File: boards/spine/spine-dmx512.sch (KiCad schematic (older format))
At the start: 20 parts, among them CON6 XLR-3 Female, Q1 DMN3190LDW, T1 10/100baseT transformer, U3 AP2204K-5.0, U5 NC7WZ14, U6 ST485E

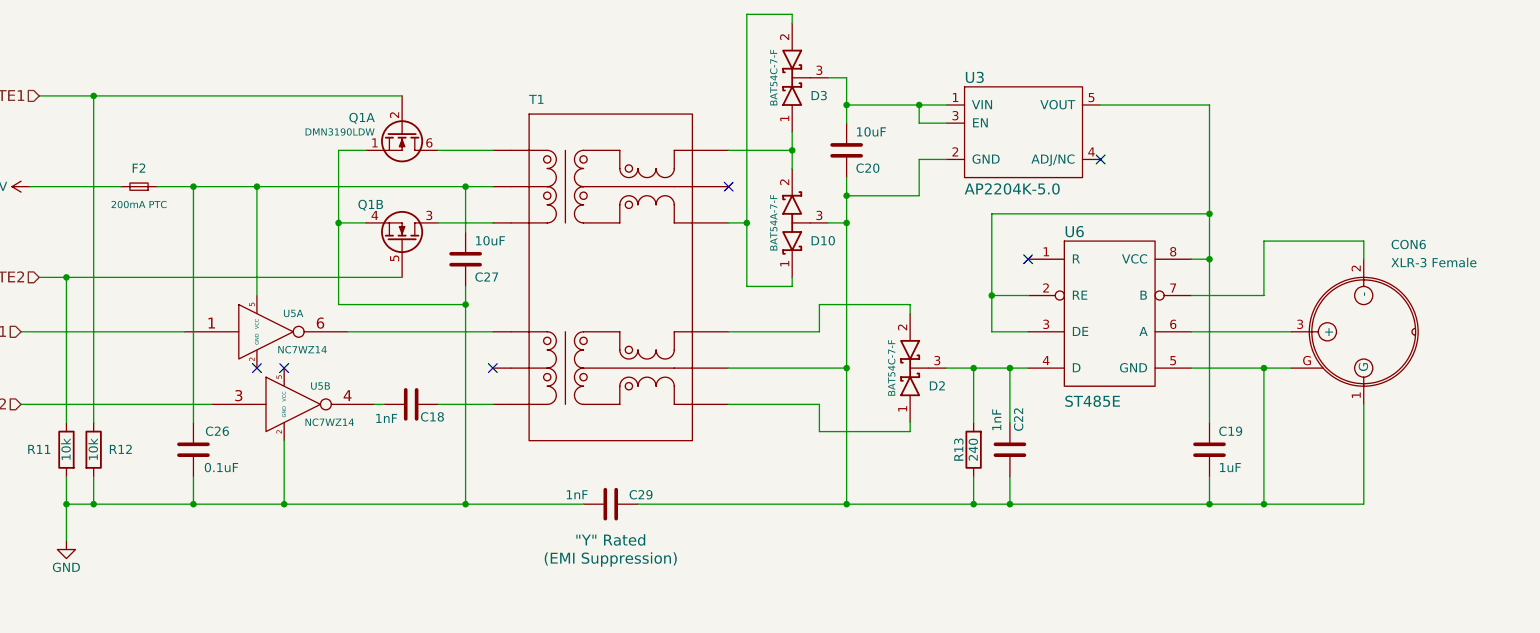
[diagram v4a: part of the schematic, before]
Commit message: Capacitor upgrades, BOM tidying
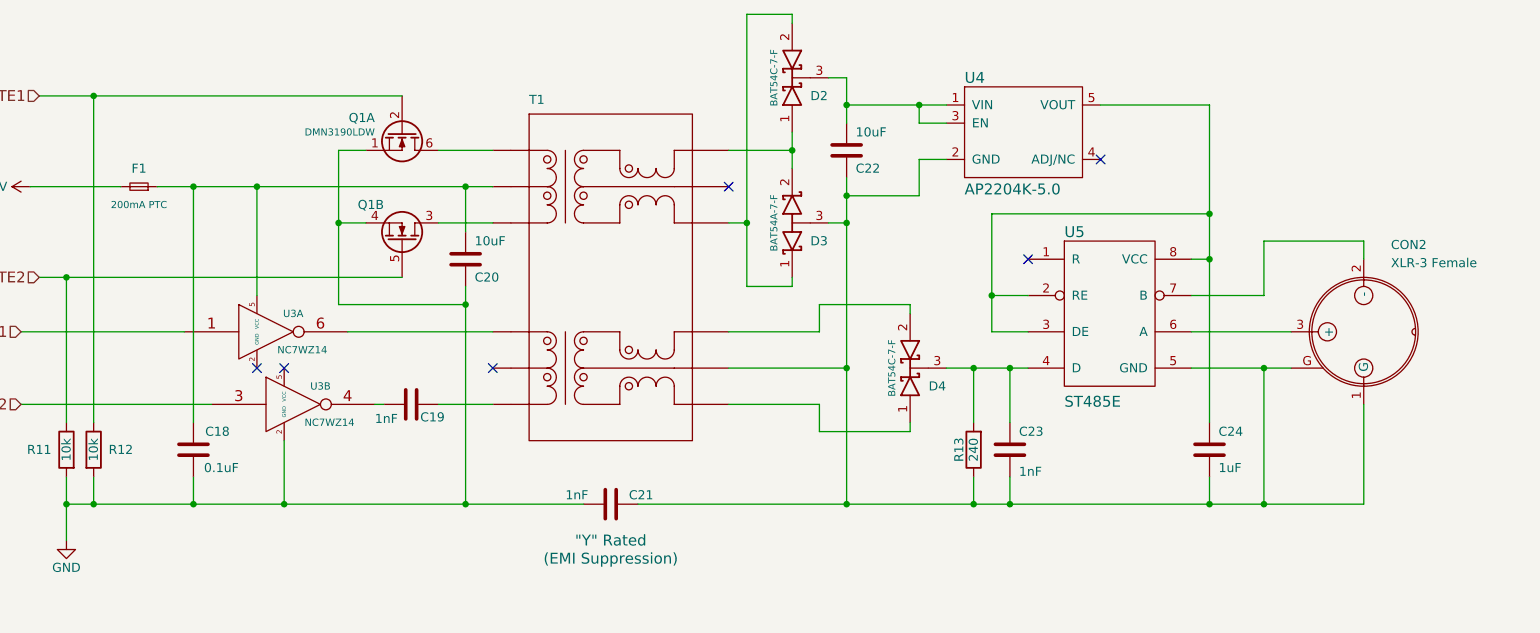
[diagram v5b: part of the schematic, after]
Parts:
- renumbered C26 to C18, C18 to C19, C27 to C20, C29 to C21, C20 to C22, C22 to C23, C19 to C24, CON6 to CON2, D3 to D2, D10 to D3, D2 to D4, F2 to F1, U5 to U3, U3 to U4, U6 to U5
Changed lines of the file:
@@
 $EndComp
 $Comp
-L C C22
+L C C23
 U 1 1 563EDC1A
 P 7200 4750
-F 0 "C22" V 7150 4850 50  0000 L CNN
-F 1 "1nF" V 7300 4850 50  0000 L BNN
+F 0 "C23" H 7150 4850 50  0000 R CNN
+F 1 "1nF" H 7150 4600 50  0000 R BNN
 F 2 "Capacitors_SMD:C_0805" H 7238 4600 30  0001 C CNN
 F 3 "http://search.murata.co.jp/Ceramy/image/img/A01X/G101/ENG/GRM216R71H102KA01-01.pdf" H 7200 4750 60  0001 C CNN
@@
 $EndComp
 $Comp
-L D_Schottky_x2_KCom_AAK D3
+L D_Schottky_x2_KCom_AAK D2
 U 1 1 563EE535
 P 6000 2700
-F 0 "D3" V 5900 2600 50  0000 R CNN
+F 0 "D2" V 5900 2600 50  0000 R CNN
 F 1 "BAT54 2x common cathode" H 6000 2800 50  0001 C CNN
 F 2 "TO_SOT_Packages_SMD:SOT-23" H 6000 2700 60  0001 C CNN
@@
 $EndComp
 $Comp
-L GND #PWR018
+L GND #PWR19
 U 1 1 563F2AEF
 P 2000 5250
-F 0 "#PWR018" H 2000 5000 50  0001 C CNN
+F 0 "#PWR19" H 2000 5000 50  0001 C CNN
 F 1 "GND" H 2000 5100 50  0000 C CNN
 F 2 "" H 2000 5250 60  0000 C CNN
@@
 TX2
 $Comp
-L NC7WZ14 U5
+L NC7WZ14 U3
 U 1 1 563F2A79
 P 3100 4100
-F 0 "U5" H 3250 4200 40  0000 C CNN
+F 0 "U3" H 3250 4200 40  0000 C CNN
 F 1 "NC7WZ14" H 3300 4000 40  0000 C CNN
 F 2 "TO_SOT_Packages_SMD:SC-70-6" H 3100 4100 60  0001 C CNN
@@
 $EndComp
 $Comp
-L NC7WZ14 U5
+L NC7WZ14 U3
 U 2 1 563F2AF3
 P 3250 4500
-F 0 "U5" H 3400 4600 40  0000 C CNN
+F 0 "U3" H 3400 4600 40  0000 C CNN
 F 1 "NC7WZ14" H 3450 4400 40  0000 C CNN
 F 2 "TO_SOT_Packages_SMD:SC-70-6" H 3250 4500 60  0001 C CNN
@@
 $EndComp
 $Comp
-L C C20
+L C C22
 U 1 1 56431ABC
 P 6300 3100
-F 0 "C20" H 6350 3000 50  0000 L CNN
+F 0 "C22" H 6350 3000 50  0000 L CNN
 F 1 "10uF" H 6350 3200 50  0000 L CNN
 F 2 "Capacitors_SMD:C_1206" H 6338 2950 30  0001 C CNN
@@
 $EndComp
 $Comp
-L C C27
+L C C20
 U 1 1 5643300D
 P 4200 3700
-F 0 "C27" H 4250 3600 50  0000 L CNN
+F 0 "C20" H 4250 3600 50  0000 L CNN
 F 1 "10uF " H 4250 3800 50  0000 L CNN
 F 2 "Capacitors_SMD:C_1206" H 4238 3550 30  0001 C CNN
@@
 $EndComp
 $Comp
-L C C26
+L C C18
 U 1 1 56433BD3
 P 2700 4750
-F 0 "C26" H 2500 4650 50  0000 L CNN
+F 0 "C18" H 2500 4650 50  0000 L CNN
 F 1 "0.1uF" H 2450 4850 50  0000 L CNN
 F 2 "Capacitors_SMD:C_0805" H 2738 4600 30  0001 C CNN
@@
 $EndComp
 $Comp
-L D_Schottky_x2_KCom_AAK D2
+L D_Schottky_x2_KCom_AAK D4
 U 1 1 564357BA
 P 6650 4300
-F 0 "D2" V 6550 4150 50  0000 C CNN
+F 0 "D4" V 6550 4150 50  0000 C CNN
 F 1 "BAT54 2x common cathode" H 6650 4400 50  0001 C CNN
 F 2 "TO_SOT_Packages_SMD:SOT-23" H 6650 4300 60  0001 C CNN
@@
 $EndComp
 $Comp
-L C C29
+L C C21
 U 1 1 564BCE29
 P 5000 5050
-F 0 "C29" V 4950 5150 50  0000 L CNN
+F 0 "C21" V 4950 5150 50  0000 L CNN
 F 1 "1nF" V 4950 4800 50  0000 L CNN
 F 2 "Capacitors_ThroughHole:C_Rect_L13_W4_P10" H 5038 4900 30  0001 C CNN
@@
 72 0F 1C A9 DC 70 49 CB 79 33 88 85 99 AD 01 6C 4B 10 FC 3B 13 DE 3B 37 68 79 AD 07 BC 00 3C 0E
 3C 31 EE E3 D8 E7 0F 03 D7 7B 9F FB C1 E1 FF 01 18 C4 96 1D B8 0E 40 07 00 00 00 00 49 45 4E 44
-AE 42 60 82 AE
+AE 42 60 82 10
 EndData
 $EndBitmap
@@
 A
 $Comp
-L F_Small F2
+L F_Small F1
 U 1 1 56760384
 P 2400 3300
-F 0 "F2" H 2400 3200 50  0000 C CNN
+F 0 "F1" H 2400 3200 50  0000 C CNN
 F 1 "200mA PTC" H 2400 3400 39  0000 C CNN
 F 2 "Resistors_SMD:R_1206" H 2400 3300 60  0001 C CNN
@@
 72 0F 1C A9 DC 70 49 CB 79 33 88 85 99 AD 01 6C 4B 10 FC 3B 13 DE 3B 37 68 79 AD 07 BC 00 3C 0E
 3C 31 EE E3 D8 E7 0F 03 D7 7B 9F FB C1 E1 FF 01 18 C4 96 1D B8 0E 40 07 00 00 00 00 49 45 4E 44
-AE 42 60 82 FF
+AE 42 60 82 00
 EndData
 $EndBitmap
@@
 A
 $Comp
-L XLR_3 CON6
+L XLR_3 CON2
 U 1 1 563E82C1
 P 9150 4100
-F 0 "CON6" V 8700 4250 50  0000 L BNN
+F 0 "CON2" V 8700 4250 50  0000 L BNN
 F 1 "XLR-3 Female" V 8800 4250 50  0000 L BNN
 F 2 "Connect:XLR3MC" H 9150 4100 60  0001 C CNN
@@
 $EndComp
 $Comp
-L SN75176B U6
+L SN75176B U5
 U 1 1 563E894A
 P 7800 3600
-F 0 "U6" H 7500 3650 60  0000 L CNN
+F 0 "U5" H 7500 3650 60  0000 L CNN
 F 1 "ST485E" H 7500 2750 60  0000 L TNN
 F 2 "Housings_SOIC:SOIC-8_3.9x4.9mm_Pitch1.27mm" H 7800 3600 60  0001 C CNN
@@
 $EndComp
 $Comp
-L D_Schottky_x2_ACom_KKA D10
+L D_Schottky_x2_ACom_KKA D3
 U 1 1 56768910
 P 6000 3500
-F 0 "D10" V 5900 3400 50  0000 R CNN
+F 0 "D3" V 5900 3400 50  0000 R CNN
 F 1 "BAT54 2x common anode" H 6000 3600 50  0001 C CNN
 F 2 "TO_SOT_Packages_SMD:SOT-23" H 6000 3500 60  0001 C CNN
@@
 $EndComp
 $Comp
-L AP2204 U3
+L AP2204 U4
 U 1 1 5676B68D
 P 7350 2850
-F 0 "U3" H 6950 3000 60  0000 L CNN
+F 0 "U4" H 6950 3000 60  0000 L CNN
 F 1 "AP2204K-5.0" H 6950 2350 60  0000 L BNN
 F 2 "TO_SOT_Packages_SMD:SOT-23-5" H 7150 3000 60  0001 C CNN
@@
 $EndComp
 $Comp
-L C C19
+L C C24
 U 1 1 5676CCD8
 P 8300 4750
-F 0 "C19" H 8350 4850 50  0000 L CNN
+F 0 "C24" H 8350 4850 50  0000 L CNN
 F 1 "1uF " H 8350 4650 50  0000 L CNN
 F 2 "Capacitors_SMD:C_0805" H 8338 4600 30  0001 C CNN
@@
 FB 59 00 E6 A5 69 3A 37 9E CF 73 BC F7 37 E3 33 5D 9E A8 3E 7F 80 FA F7 F6 BB 44 F4 6E D4 E7 77
 A2 1E 1F 27 A2 E3 16 70 32 E9 54 FE 3F E7 AF 00 CA 1C A3 36 0A 00 00 00 00 49 45 4E 44 AE 42 60
-82 00
+82 70
 EndData
 $EndBitmap
@@
 72 0F 1C A9 DC 70 49 CB 79 33 88 85 99 AD 01 6C 4B 10 FC 3B 13 DE 3B 37 68 79 AD 07 BC 00 3C 0E
 3C 31 EE E3 D8 E7 0F 03 D7 7B 9F FB C1 E1 FF 01 18 C4 96 1D B8 0E 40 07 00 00 00 00 49 45 4E 44
-AE 42 60 82 FF
+AE 42 60 82 00
 EndData
 $EndBitmap
@@
 NoConn ~ 4350 4300
 $Comp
-L C C18
+L C C19
 U 1 1 5677875C
 P 3900 4500
-F 0 "C18" V 3800 4550 50  0000 L TNN
+F 0 "C19" V 3800 4550 50  0000 L TNN
 F 1 "1nF" V 3850 4300 50  0000 L BNN
 F 2 "Capacitors_SMD:C_0805" H 3938 4350 30  0001 C CNN
@@
 $EndComp
 $Comp
-L +5V #PWR019
+L +5V #PWR18
 U 1 1 5678642B
 P 1800 3300
-F 0 "#PWR019" H 1800 3150 50  0001 C CNN
+F 0 "#PWR18" H 1800 3150 50  0001 C CNN
 F 1 "+5V" V 1800 3500 50  0000 C CNN
 F 2 "" H 1800 3300 60  0000 C CNN

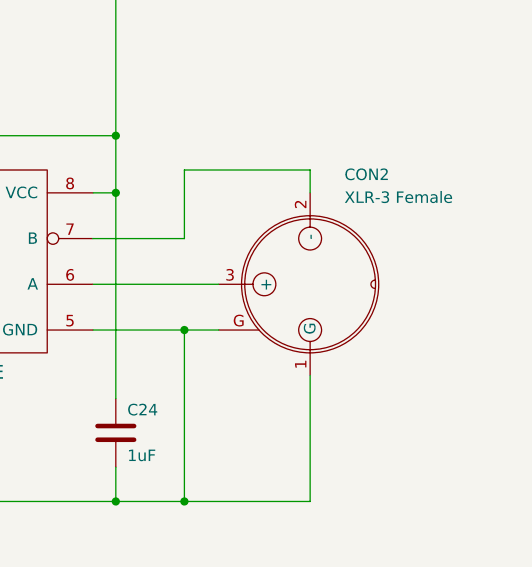
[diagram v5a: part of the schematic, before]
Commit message: About 50% dimmer blue LED when FPGA is unconfigured
This seems a good compromise between visibility while debugging and unobtrusiveness during normal operation.
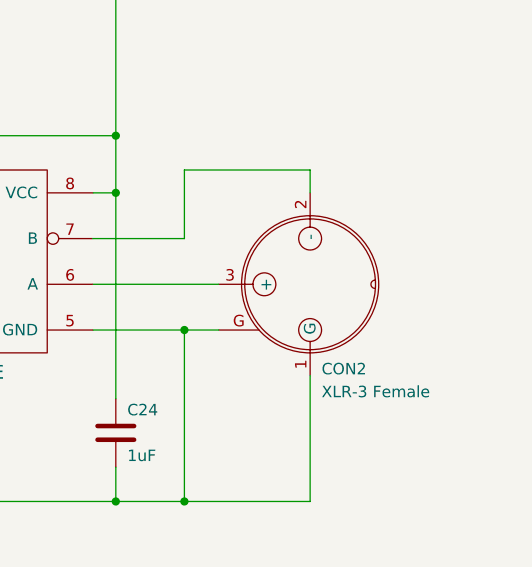
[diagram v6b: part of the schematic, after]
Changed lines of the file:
@@
 $EndComp
 $Comp
-L GND #PWR19
+L GND #PWR018
 U 1 1 563F2AEF
 P 2000 5250
-F 0 "#PWR19" H 2000 5000 50  0001 C CNN
+F 0 "#PWR018" H 2000 5000 50  0001 C CNN
 F 1 "GND" H 2000 5100 50  0000 C CNN
 F 2 "" H 2000 5250 60  0000 C CNN
@@
 72 0F 1C A9 DC 70 49 CB 79 33 88 85 99 AD 01 6C 4B 10 FC 3B 13 DE 3B 37 68 79 AD 07 BC 00 3C 0E
 3C 31 EE E3 D8 E7 0F 03 D7 7B 9F FB C1 E1 FF 01 18 C4 96 1D B8 0E 40 07 00 00 00 00 49 45 4E 44
-AE 42 60 82 10
+AE 42 60 82 4D
 EndData
 $EndBitmap
@@
 72 0F 1C A9 DC 70 49 CB 79 33 88 85 99 AD 01 6C 4B 10 FC 3B 13 DE 3B 37 68 79 AD 07 BC 00 3C 0E
 3C 31 EE E3 D8 E7 0F 03 D7 7B 9F FB C1 E1 FF 01 18 C4 96 1D B8 0E 40 07 00 00 00 00 49 45 4E 44
-AE 42 60 82 00
+AE 42 60 82 4D
 EndData
 $EndBitmap
@@
 U 1 1 563E82C1
 P 9150 4100
-F 0 "CON2" V 8700 4250 50  0000 L BNN
-F 1 "XLR-3 Female" V 8800 4250 50  0000 L BNN
+F 0 "CON2" V 9550 4150 50  0000 L BNN
+F 1 "XLR-3 Female" V 9650 4150 50  0000 L BNN
 F 2 "Connect:XLR3MC" H 9150 4100 60  0001 C CNN
 F 3 "http://www.neutrik.us/en-us/xlr/aa-series/nc3faah2-0" H 9150 4100 60  0001 C CNN
@@
 FB 59 00 E6 A5 69 3A 37 9E CF 73 BC F7 37 E3 33 5D 9E A8 3E 7F 80 FA F7 F6 BB 44 F4 6E D4 E7 77
 A2 1E 1F 27 A2 E3 16 70 32 E9 54 FE 3F E7 AF 00 CA 1C A3 36 0A 00 00 00 00 49 45 4E 44 AE 42 60
-82 70
+82 00
 EndData
 $EndBitmap
@@
 $EndComp
 $Comp
-L +5V #PWR18
+L +5V #PWR019
 U 1 1 5678642B
 P 1800 3300
-F 0 "#PWR18" H 1800 3150 50  0001 C CNN
+F 0 "#PWR019" H 1800 3150 50  0001 C CNN
 F 1 "+5V" V 1800 3500 50  0000 C CNN
 F 2 "" H 1800 3300 60  0000 C CNN
